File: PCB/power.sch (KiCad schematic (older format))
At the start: 42 parts, among them J1 4DB-P108-06, J2 039531-1002, U4 LDLN030G33R, U5 TPS54308

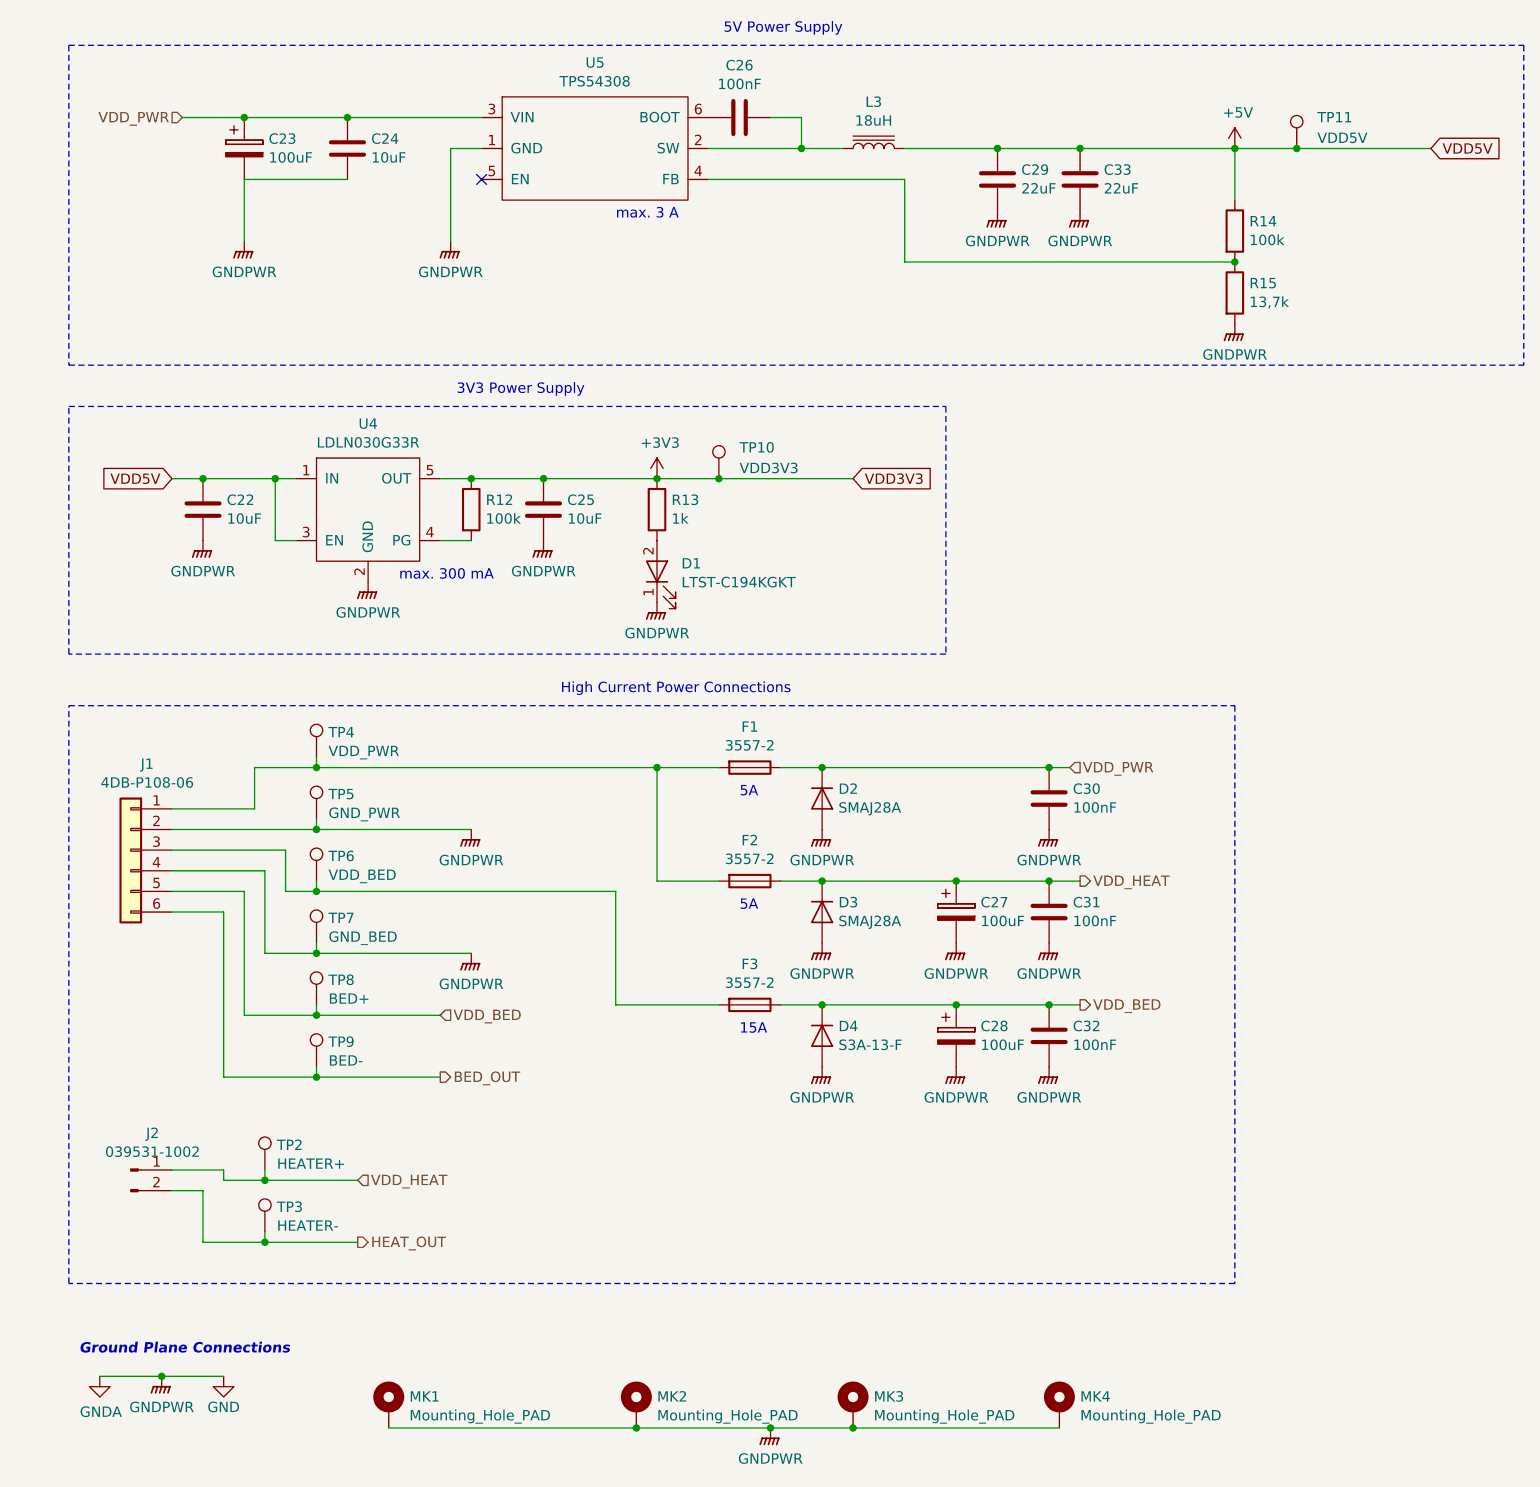
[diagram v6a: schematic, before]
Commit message: Saving work in progress.
Every component now has a 3D mode.
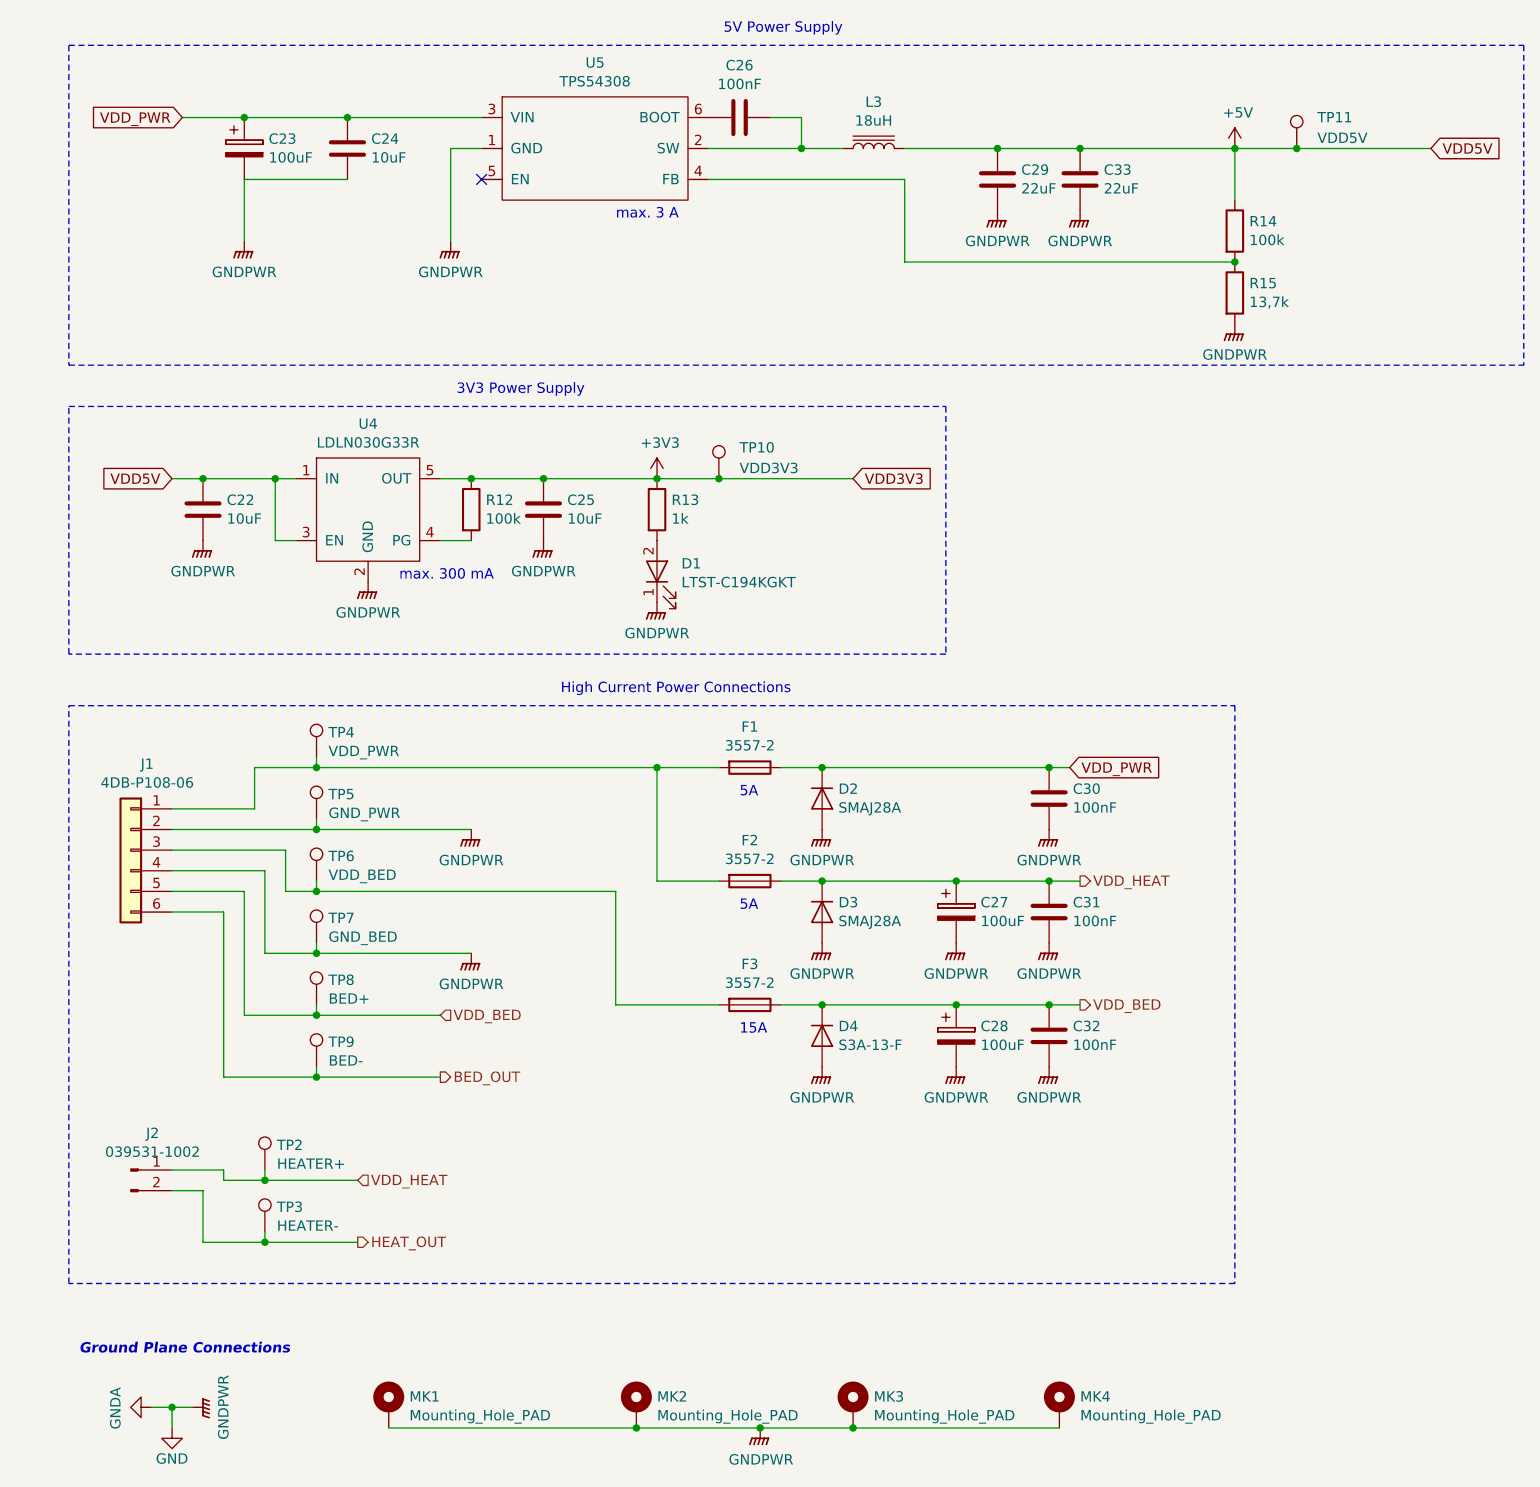
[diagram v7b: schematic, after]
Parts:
- L3: footprint Inductor_SMD:L_Wuerth_WE-PDF -> custom-footprints:L_Wuerth_WE-PDF; Notice (none) -> 7447798181
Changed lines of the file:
@@
 F 0 "L3" V 4825 1150 50  0000 C CNN
 F 1 "18uH" V 4734 1150 50  0000 C CNN
-F 2 "Inductor_SMD:L_Wuerth_WE-PDF" H 4600 1150 50  0001 C CNN
+F 2 "custom-footprints:L_Wuerth_WE-PDF" H 4600 1150 50  0001 C CNN
 F 3 "https://www.mouser.com/datasheet/2/445/7447798181-539715.pdf" H 4600 1150 50  0001 C CNN
+F 4 "7447798181" V 4600 1150 50  0001 C CNN "Notice"
 	1    4600 1150
 	0    -1   -1   0
@@
 L power:GNDPWR #PWR024
 U 1 1 5AFD7C84
-P 1150 7100
-F 0 "#PWR024" H 1150 6900 50  0001 C CNN
-F 1 "GNDPWR" H 1150 6950 50  0000 C CNN
-F 2 "" H 1150 7050 50  0001 C CNN
-F 3 "" H 1150 7050 50  0001 C CNN
-	1    1150 7100
-	1    0    0    -1
+P 1300 7250
+F 0 "#PWR024" H 1300 7050 50  0001 C CNN
+F 1 "GNDPWR" H 1300 7100 50  0000 C CNN
+F 2 "" H 1300 7200 50  0001 C CNN
+F 3 "" H 1300 7200 50  0001 C CNN
+	1    1300 7250
+	0    -1   -1   0
 $EndComp
 $Comp
 L power:GND #PWR026
 U 1 1 5AFD7DB1
-P 1450 7100
-F 0 "#PWR026" H 1450 6850 50  0001 C CNN
-F 1 "GND" H 1450 6950 50  0000 C CNN
-F 2 "" H 1450 7100 50  0001 C CNN
-F 3 "" H 1450 7100 50  0001 C CNN
-	1    1450 7100
-	1    0    0    -1
-$EndComp
-Wire Wire Line
-	1150 7100 1450 7100
+P 1200 7350
+F 0 "#PWR026" H 1200 7100 50  0001 C CNN
+F 1 "GND" H 1200 7200 50  0000 C CNN
+F 2 "" H 1200 7350 50  0001 C CNN
+F 3 "" H 1200 7350 50  0001 C CNN
+	1    1200 7350
+	1    0    0    -1
+$EndComp
 Text Notes 750  7000 0    50   Italic 10
 Ground Plane Connections
@@
 L power:GNDA #PWR023
 U 1 1 5B058B1E
-P 850 7100
-F 0 "#PWR023" H 850 6850 50  0001 C CNN
-F 1 "GNDA" H 855 6927 50  0000 C CNN
-F 2 "" H 850 7100 50  0001 C CNN
-F 3 "" H 850 7100 50  0001 C CNN
-	1    850  7100
-	1    0    0    -1
-$EndComp
-Wire Wire Line
-	850  7100 1150 7100
-Connection ~ 1150 7100
+P 1100 7250
+F 0 "#PWR023" H 1100 7000 50  0001 C CNN
+F 1 "GNDA" H 1105 7077 50  0000 C CNN
+F 2 "" H 1100 7250 50  0001 C CNN
+F 3 "" H 1100 7250 50  0001 C CNN
+	1    1100 7250
+	0    1    1    0
+$EndComp
 Connection ~ 4350 5300
 Wire Wire Line
@@
 	2100 6150 1650 6150
 Wire Wire Line
-	1450 6150 1450 6100
-Wire Wire Line
-	1450 6100 1200 6100
-Wire Wire Line
 	1650 6150 1650 6100
 Connection ~ 1650 6150
@@
 Wire Wire Line
 	2100 6450 1650 6450
-Wire Wire Line
-	1350 6450 1350 6200
-Wire Wire Line
-	1350 6200 1200 6200
 Wire Wire Line
 	1650 6400 1650 6450
@@
 	1    0    0    -1
 $EndComp
-$Comp
-L power:GNDPWR #PWR035
-U 1 1 5B0578CF
-P 4100 7350
-F 0 "#PWR035" H 4100 7150 50  0001 C CNN
-F 1 "GNDPWR" H 4100 7200 50  0000 C CNN
-F 2 "" H 4100 7300 50  0001 C CNN
-F 3 "" H 4100 7300 50  0001 C CNN
-	1    4100 7350
-	1    0    0    -1
-$EndComp
-Wire Wire Line
-	5500 7350 4500 7350
-Connection ~ 3450 7350
-Wire Wire Line
-	3450 7350 2250 7350
-Connection ~ 4100 7350
-Wire Wire Line
-	4100 7350 3450 7350
-Connection ~ 4500 7350
-Wire Wire Line
-	4500 7350 4100 7350
 NoConn ~ 2700 1300
-Text HLabel 5550 4150 2    50   Input ~ 0
-VDD_PWR
-Text HLabel 1250 1000 0    50   Input ~ 0
-VDD_PWR
 $Comp
 L power:+5V #PWR046
@@
 Wire Wire Line
 	1550 1000 2050 1000
+Wire Wire Line
+	1100 7250 1200 7250
+Wire Wire Line
+	1200 7350 1200 7250
+Connection ~ 1200 7250
+Wire Wire Line
+	1200 7250 1300 7250
+$Comp
+L power:GNDPWR #PWR0152
+U 1 1 5AFCD887
+P 4050 7350
+F 0 "#PWR0152" H 4050 7150 50  0001 C CNN
+F 1 "GNDPWR" H 4054 7196 50  0000 C CNN
+F 2 "" H 4050 7300 50  0001 C CNN
+F 3 "" H 4050 7300 50  0001 C CNN
+	1    4050 7350
+	1    0    0    -1
+$EndComp
+Wire Wire Line
+	5500 7350 4500 7350
+Connection ~ 3450 7350
+Wire Wire Line
+	3450 7350 2250 7350
+Connection ~ 4050 7350
+Wire Wire Line
+	4050 7350 3450 7350
+Connection ~ 4500 7350
+Wire Wire Line
+	4500 7350 4050 7350
+Text GLabel 5550 4150 2    50   Input ~ 0
+VDD_PWR
+Text GLabel 1250 1000 0    50   Input ~ 0
+VDD_PWR
+Wire Wire Line
+	1450 6150 1450 6100
+Wire Wire Line
+	1350 6450 1350 6200
+Wire Wire Line
+	1350 6200 1200 6200
+Wire Wire Line
+	1450 6100 1200 6100
 $EndSCHEMATC

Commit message: Removed logic level converter. Changed LDO.
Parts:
- removed R12: 100k, Resistor_SMD:R_0603_1608Metric, symbol Device:R
- removed U4: LDLN030G33R, Package_TO_SOT_SMD:TSOT-23-5, symbol remram-custom:LDLN030G33R
- added U2: AP2112K-3.3TRG1, Package_TO_SOT_SMD:SOT-23-5, symbol remram-custom:AP2112K-3.3TRG1
- renumbered C26 to C1, C31 to C10, C28 to C11, C32 to C12, C23 to C2, C24 to C3, C29 to C4, C33 to C5, C22 to C6, C25 to C7, C30 to C8, C27 to C9, L3 to L1, R14 to R1, R15 to R2, R13 to R3, TP11 to TP1, TP3 to TP10, TP10 to TP2, TP4 to TP3, TP5 to TP4, TP6 to TP5, TP7 to TP6, TP8 to TP7, TP9 to TP8, TP2 to TP9, U5 to U1
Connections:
- wire segments 92 -> 90
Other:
- note added: "min. 600 mA"
- note removed: "max. 300 mA"
- moved on the sheet: C7
